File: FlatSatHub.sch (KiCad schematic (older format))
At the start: 15 parts, among them J1 Jack-DC, SW1 SW_DIP_x02, SW10 SW_SPST

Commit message: route and add documentation for schematic
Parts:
- gave numbers to parts that had none: 6
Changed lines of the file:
@@
 F 1 "bel-xRBA-06E2Ax" H 9025 2250 50  0000 L CNN
 F 2 "FlatSatHub:BEL-xRBA-06E2Ax" H 9750 2125 50  0001 C CNN
-F 3 "" H 9750 2125 50  0001 C CNN
+F 3 "https://www.mouser.fr/ProductDetail/Bel-Fuse/SRBA-06E2ALG?qs=sGAEpiMZZMsc0tfZmXiUnbbQTgs0Rw32i9gRZ8J9EPVOGBp8LJLa%2Fg%3D%3D" H 9750 2125 50  0001 C CNN
 	1    9450 1925
 	-1   0    0    1
@@
 F 1 "CINCON-SIPSMT10-12" H 9000 3400 50  0000 L CNN
 F 2 "FlatSatHub:CINCON-SIPSMT10-12" H 10050 3150 50  0001 C CNN
-F 3 "" H 10050 3150 50  0001 C CNN
+F 3 "https://www.mouser.fr/ProductDetail/Cincon/SIP10-12S33?qs=sGAEpiMZZMsc0tfZmXiUnRxObuznqcoYDYuJZBYUaXE=" H 10050 3150 50  0001 C CNN
 	1    9500 3000
 	-1   0    0    1
@@
 $EndComp
 $Comp
-L Device:LED D?
+L Device:LED D3
 U 1 1 5F2D3A02
 P 7850 1600
-F 0 "D?" H 7843 1345 50  0000 C CNN
+F 0 "D3" H 7843 1345 50  0000 C CNN
 F 1 "LED" H 7843 1436 50  0000 C CNN
 F 2 "" H 7850 1600 50  0001 C CNN
@@
 $EndComp
 $Comp
-L Device:LED D?
+L Device:LED D1
 U 1 1 5F2D4A24
 P 7825 2250
-F 0 "D?" H 7818 1995 50  0000 C CNN
+F 0 "D1" H 7818 1995 50  0000 C CNN
 F 1 "LED" H 7818 2086 50  0000 C CNN
 F 2 "" H 7825 2250 50  0001 C CNN
@@
 $EndComp
 $Comp
-L Device:LED D?
+L Device:LED D2
 U 1 1 5F2DEAA8
 P 7825 2575
-F 0 "D?" H 7818 2320 50  0000 C CNN
+F 0 "D2" H 7818 2320 50  0000 C CNN
 F 1 "LED" H 7818 2411 50  0000 C CNN
 F 2 "" H 7825 2575 50  0001 C CNN
@@
 $EndComp
 $Comp
-L Device:R R?
+L Device:R R3
 U 1 1 5F2E82E2
 P 8150 1600
-F 0 "R?" V 7943 1600 50  0000 C CNN
+F 0 "R3" V 7943 1600 50  0000 C CNN
 F 1 "R" V 8034 1600 50  0000 C CNN
 F 2 "" V 8080 1600 50  0001 C CNN
@@
 $EndComp
 $Comp
-L Device:R R?
+L Device:R R1
 U 1 1 5F2E9255
 P 8125 2250
-F 0 "R?" V 7918 2250 50  0000 C CNN
+F 0 "R1" V 7918 2250 50  0000 C CNN
 F 1 "R" V 8009 2250 50  0000 C CNN
 F 2 "" V 8055 2250 50  0001 C CNN
@@
 $EndComp
 $Comp
-L Device:R R?
+L Device:R R2
 U 1 1 5F2F2A98
 P 8125 2575
-F 0 "R?" V 7918 2575 50  0000 C CNN
+F 0 "R2" V 7918 2575 50  0000 C CNN
 F 1 "R" V 8009 2575 50  0000 C CNN
 F 2 "" V 8055 2575 50  0001 C CNN
@@
 $EndComp
 $Comp
-L power:GND #PWR?
+L power:GND #PWR0101
 U 1 1 5F2FC3AF
 P 8300 1600
-F 0 "#PWR?" H 8300 1350 50  0001 C CNN
+F 0 "#PWR0101" H 8300 1350 50  0001 C CNN
 F 1 "GND" V 8305 1472 50  0000 R CNN
 F 2 "" H 8300 1600 50  0001 C CNN
@@
 $EndComp
 $Comp
-L power:GND #PWR?
+L power:GND #PWR0104
 U 1 1 5F2FCCF0
 P 8275 2250
-F 0 "#PWR?" H 8275 2000 50  0001 C CNN
+F 0 "#PWR0104" H 8275 2000 50  0001 C CNN
 F 1 "GND" V 8280 2122 50  0000 R CNN
 F 2 "" H 8275 2250 50  0001 C CNN
@@
 $EndComp
 $Comp
-L power:GND #PWR?
+L power:GND #PWR0107
 U 1 1 5F3063BD
 P 8275 2575
-F 0 "#PWR?" H 8275 2325 50  0001 C CNN
+F 0 "#PWR0107" H 8275 2325 50  0001 C CNN
 F 1 "GND" V 8280 2447 50  0000 R CNN
 F 2 "" H 8275 2575 50  0001 C CNN

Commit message: Change DB-26-HD footprint to match what we want
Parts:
- D1, D2, D3: footprint (none) -> LED_SMD:LED_0603_1608Metric_Pad1.05x0.95mm_HandSolder
- R1, R2, R3: footprint (none) -> Resistor_SMD:R_0603_1608Metric_Pad1.05x0.95mm_HandSolder
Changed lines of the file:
@@
 F 0 "D3" H 7843 1345 50  0000 C CNN
 F 1 "LED" H 7843 1436 50  0000 C CNN
-F 2 "" H 7850 1600 50  0001 C CNN
+F 2 "LED_SMD:LED_0603_1608Metric_Pad1.05x0.95mm_HandSolder" H 7850 1600 50  0001 C CNN
 F 3 "~" H 7850 1600 50  0001 C CNN
 	1    7850 1600
@@
 F 0 "D1" H 7818 1995 50  0000 C CNN
 F 1 "LED" H 7818 2086 50  0000 C CNN
-F 2 "" H 7825 2250 50  0001 C CNN
+F 2 "LED_SMD:LED_0603_1608Metric_Pad1.05x0.95mm_HandSolder" H 7825 2250 50  0001 C CNN
 F 3 "~" H 7825 2250 50  0001 C CNN
 	1    7825 2250
@@
 F 0 "D2" H 7818 2320 50  0000 C CNN
 F 1 "LED" H 7818 2411 50  0000 C CNN
-F 2 "" H 7825 2575 50  0001 C CNN
+F 2 "LED_SMD:LED_0603_1608Metric_Pad1.05x0.95mm_HandSolder" H 7825 2575 50  0001 C CNN
 F 3 "~" H 7825 2575 50  0001 C CNN
 	1    7825 2575
@@
 F 0 "R3" V 7943 1600 50  0000 C CNN
 F 1 "R" V 8034 1600 50  0000 C CNN
-F 2 "" V 8080 1600 50  0001 C CNN
+F 2 "Resistor_SMD:R_0603_1608Metric_Pad1.05x0.95mm_HandSolder" V 8080 1600 50  0001 C CNN
 F 3 "~" H 8150 1600 50  0001 C CNN
 	1    8150 1600
@@
 F 0 "R1" V 7918 2250 50  0000 C CNN
 F 1 "R" V 8009 2250 50  0000 C CNN
-F 2 "" V 8055 2250 50  0001 C CNN
+F 2 "Resistor_SMD:R_0603_1608Metric_Pad1.05x0.95mm_HandSolder" V 8055 2250 50  0001 C CNN
 F 3 "~" H 8125 2250 50  0001 C CNN
 	1    8125 2250
@@
 F 0 "R2" V 7918 2575 50  0000 C CNN
 F 1 "R" V 8009 2575 50  0000 C CNN
-F 2 "" V 8055 2575 50  0001 C CNN
+F 2 "Resistor_SMD:R_0603_1608Metric_Pad1.05x0.95mm_HandSolder" V 8055 2575 50  0001 C CNN
 F 3 "~" H 8125 2575 50  0001 C CNN
 	1    8125 2575

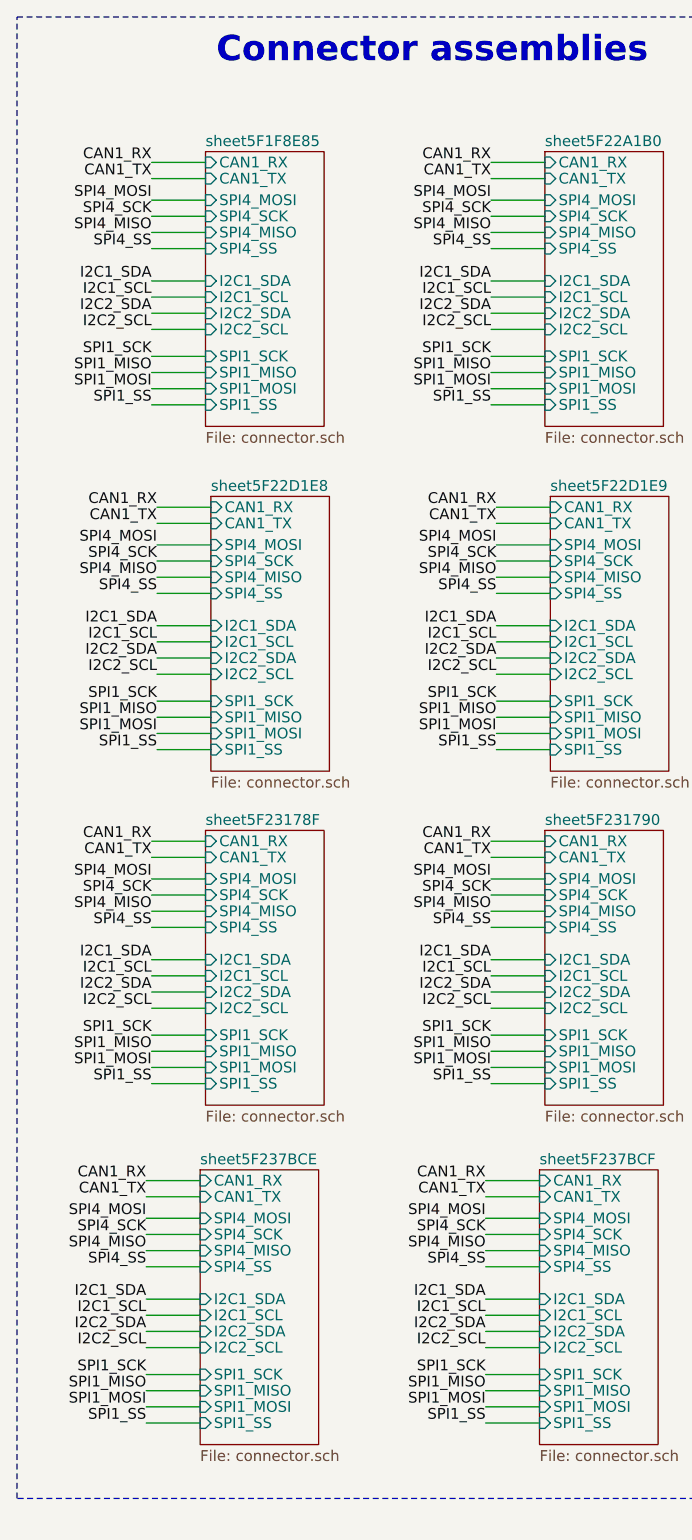
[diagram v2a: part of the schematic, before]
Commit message: new UART layout and rewire
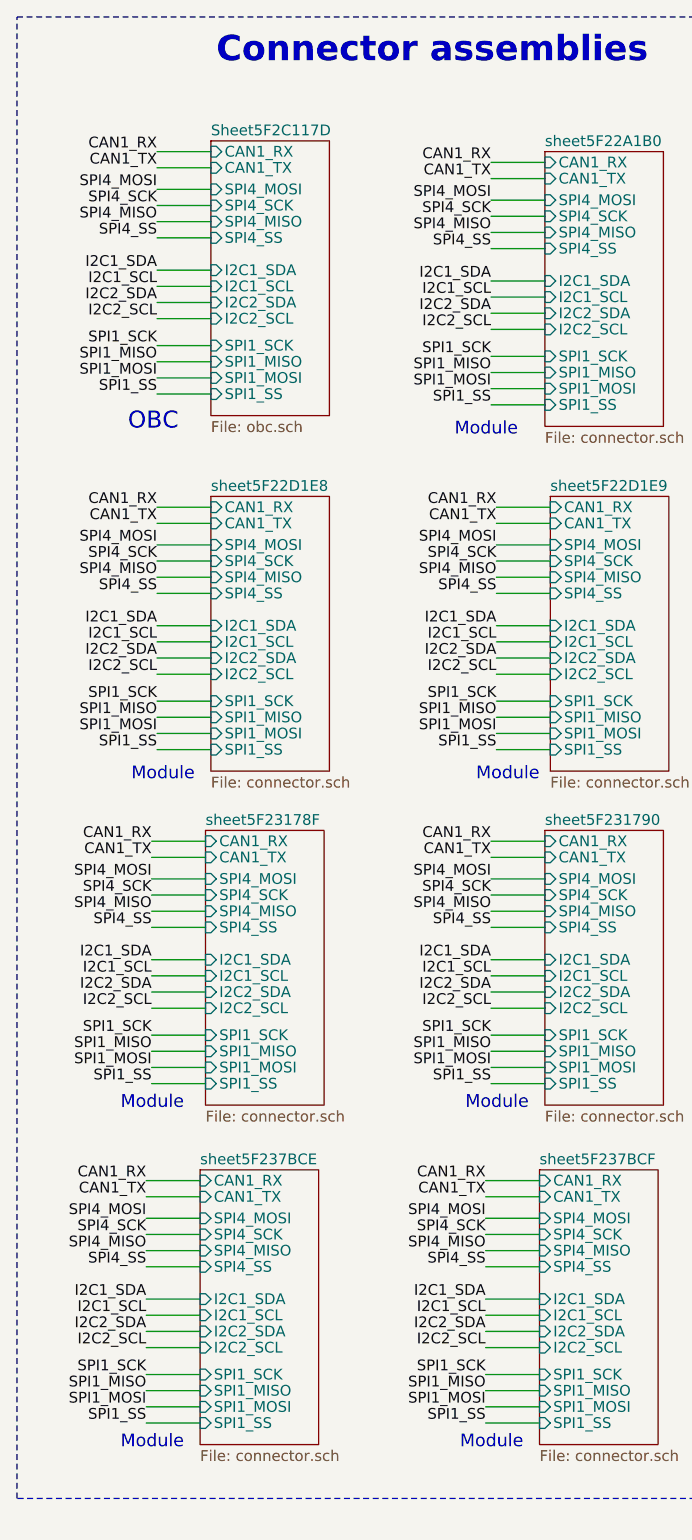
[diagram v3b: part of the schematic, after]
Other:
- note added: "Module"
- note added: "OBC"
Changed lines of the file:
@@
 $EndBitmap
-Wire Wire Line
-	1675 2450 1925 2450
-Wire Wire Line
-	1675 2375 1925 2375
-Wire Wire Line
-	1925 2300 1675 2300
-Wire Wire Line
-	1675 2225 1925 2225
-Wire Wire Line
-	1675 2100 1925 2100
-Wire Wire Line
-	1675 2025 1925 2025
-Wire Wire Line
-	1675 1950 1925 1950
-Wire Wire Line
-	1675 1875 1925 1875
-Wire Wire Line
-	1675 1725 1925 1725
-Wire Wire Line
-	1675 1650 1925 1650
-Wire Wire Line
-	1675 1575 1925 1575
-Wire Wire Line
-	1675 1500 1925 1500
-Wire Wire Line
-	1675 1400 1925 1400
-Wire Wire Line
-	1675 1325 1925 1325
-$Sheet
-S 1925 1275 550  1275
-U 5F1F8EB1
-F0 "sheet5F1F8E85" 50
-F1 "connector.sch" 50
-F2 "I2C1_SDA" I L 1925 1875 50
-F3 "I2C1_SCL" I L 1925 1950 50
-F4 "I2C2_SDA" I L 1925 2025 50
-F5 "SPI1_SCK" I L 1925 2225 50
-F6 "I2C2_SCL" I L 1925 2100 50
-F7 "SPI1_MISO" I L 1925 2300 50
-F8 "SPI1_MOSI" I L 1925 2375 50
-F9 "SPI4_SCK" I L 1925 1575 50
-F10 "SPI4_MISO" I L 1925 1650 50
-F11 "CAN1_RX" I L 1925 1325 50
-F12 "CAN1_TX" I L 1925 1400 50
-F13 "SPI4_MOSI" I L 1925 1500 50
-F14 "SPI1_SS" I L 1925 2450 50
-F15 "SPI4_SS" I L 1925 1725 50
-$EndSheet
-Text Label 1675 1325 2    50   ~ 0
-CAN1_RX
-Text Label 1675 1400 2    50   ~ 0
-CAN1_TX
-Text Label 1675 1500 2    50   ~ 0
-SPI4_MOSI
-Text Label 1675 1575 2    50   ~ 0
-SPI4_SCK
-Text Label 1675 1650 2    50   ~ 0
-SPI4_MISO
-Text Label 1675 1725 2    50   ~ 0
-SPI4_SS
-Text Label 1675 1875 2    50   ~ 0
-I2C1_SDA
-Text Label 1675 1950 2    50   ~ 0
-I2C1_SCL
-Text Label 1675 2025 2    50   ~ 0
-I2C2_SDA
-Text Label 1675 2100 2    50   ~ 0
-I2C2_SCL
-Text Label 1675 2225 2    50   ~ 0
-SPI1_SCK
-Text Label 1675 2300 2    50   ~ 0
-SPI1_MISO
-Text Label 1675 2375 2    50   ~ 0
-SPI1_MOSI
-Text Label 1675 2450 2    50   ~ 0
-SPI1_SS
 Wire Wire Line
 	3250 2450 3500 2450
@@
 Wire Wire Line
 	7600 2450 7525 2450
+Wire Wire Line
+	1700 2400 1950 2400
+Wire Wire Line
+	1700 2325 1950 2325
+Wire Wire Line
+	1950 2250 1700 2250
+Wire Wire Line
+	1700 2175 1950 2175
+Wire Wire Line
+	1700 2050 1950 2050
+Wire Wire Line
+	1700 1975 1950 1975
+Wire Wire Line
+	1700 1900 1950 1900
+Wire Wire Line
+	1700 1825 1950 1825
+Wire Wire Line
+	1700 1675 1950 1675
+Wire Wire Line
+	1700 1600 1950 1600
+Wire Wire Line
+	1700 1525 1950 1525
+Wire Wire Line
+	1700 1450 1950 1450
+Wire Wire Line
+	1700 1350 1950 1350
+Wire Wire Line
+	1700 1275 1950 1275
+Text Label 1700 1275 2    50   ~ 0
+CAN1_RX
+Text Label 1700 1350 2    50   ~ 0
+CAN1_TX
+Text Label 1700 1450 2    50   ~ 0
+SPI4_MOSI
+Text Label 1700 1525 2    50   ~ 0
+SPI4_SCK
+Text Label 1700 1600 2    50   ~ 0
+SPI4_MISO
+Text Label 1700 1675 2    50   ~ 0
+SPI4_SS
+Text Label 1700 1825 2    50   ~ 0
+I2C1_SDA
+Text Label 1700 1900 2    50   ~ 0
+I2C1_SCL
+Text Label 1700 1975 2    50   ~ 0
+I2C2_SDA
+Text Label 1700 2050 2    50   ~ 0
+I2C2_SCL
+Text Label 1700 2175 2    50   ~ 0
+SPI1_SCK
+Text Label 1700 2250 2    50   ~ 0
+SPI1_MISO
+Text Label 1700 2325 2    50   ~ 0
+SPI1_MOSI
+Text Label 1700 2400 2    50   ~ 0
+SPI1_SS
+$Sheet
+S 1950 1225 550  1275
+U 5F2C117D
+F0 "Sheet5F2C117D" 50
+F1 "obc.sch" 50
+F2 "I2C1_SDA" I L 1950 1825 50
+F3 "I2C1_SCL" I L 1950 1900 50
+F4 "I2C2_SDA" I L 1950 1975 50
+F5 "SPI1_SCK" I L 1950 2175 50
+F6 "I2C2_SCL" I L 1950 2050 50
+F7 "SPI1_MISO" I L 1950 2250 50
+F8 "SPI1_MOSI" I L 1950 2325 50
+F9 "SPI4_SCK" I L 1950 1525 50
+F10 "SPI4_MISO" I L 1950 1600 50
+F11 "CAN1_RX" I L 1950 1275 50
+F12 "CAN1_TX" I L 1950 1350 50
+F13 "SPI4_MOSI" I L 1950 1450 50
+F14 "SPI1_SS" I L 1950 2400 50
+F15 "SPI4_SS" I L 1950 1675 50
+$EndSheet
+Text Notes 1800 2575 2    79   ~ 0
+OBC
+Text Notes 3375 2600 2    59   ~ 0
+Module
+Text Notes 3475 4200 2    59   ~ 0
+Module
+Text Notes 1875 4200 2    59   ~ 0
+Module
+Text Notes 3425 5725 2    59   ~ 0
+Module
+Text Notes 1825 5725 2    59   ~ 0
+Module
+Text Notes 1825 7300 2    59   ~ 0
+Module
+Text Notes 3400 7300 2    59   ~ 0
+Module
 $EndSCHEMATC

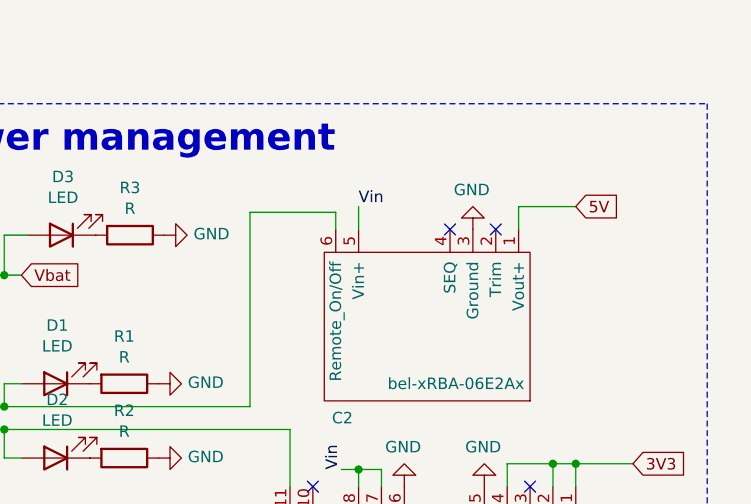
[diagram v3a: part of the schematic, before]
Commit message: fix dc converter wiring and gnd track size
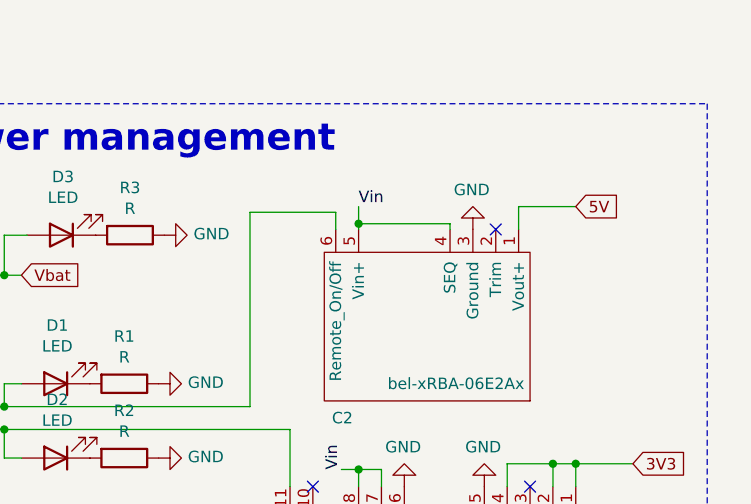
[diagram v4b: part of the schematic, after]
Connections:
- net Vin: now also C2.4 (SEQ)
- no-connect marks 4 -> 3
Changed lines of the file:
@@
 	9150 2700 9150 2625
 Wire Wire Line
-	9150 1575 9150 1475
+	9150 1575 9150 1550
 Wire Wire Line
 	9250 2625 9150 2625
@@
 	9850 1475 10100 1475
 NoConn ~ 9750 1575
-NoConn ~ 9550 1575
 $Comp
 L power:GND #PWR010
@@
 Text Notes 3400 7300 2    59   ~ 0
 Module
+Wire Wire Line
+	9150 1550 9550 1550
+Wire Wire Line
+	9550 1550 9550 1575
+Connection ~ 9150 1550
+Wire Wire Line
+	9150 1550 9150 1475
 $EndSCHEMATC

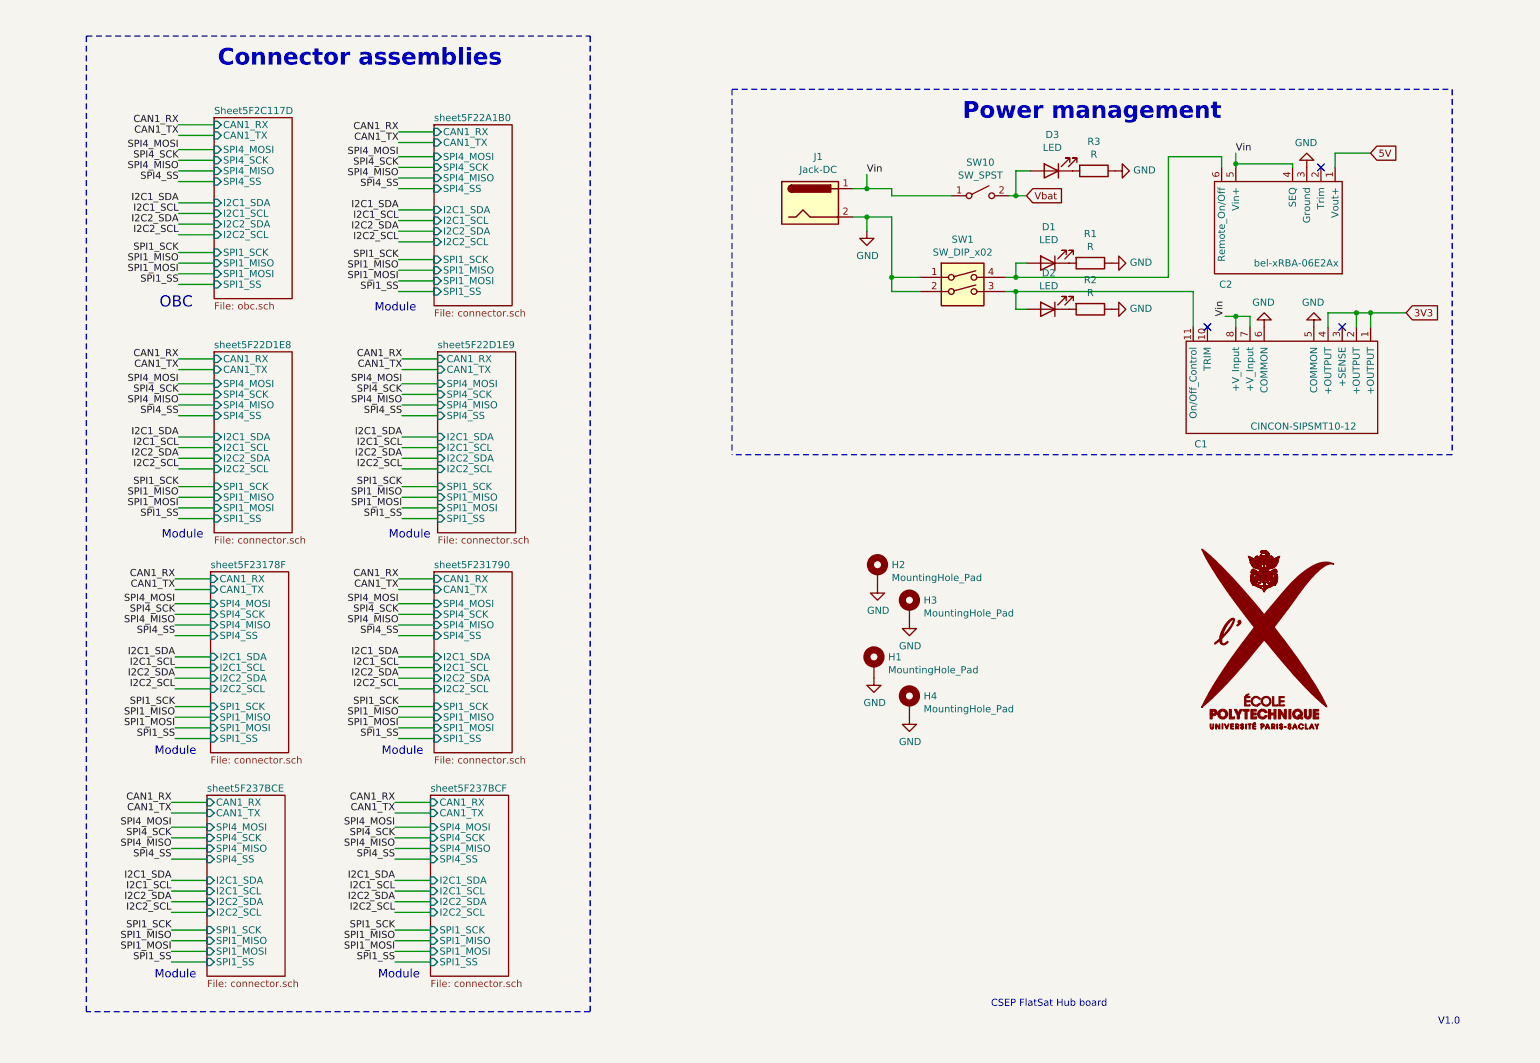
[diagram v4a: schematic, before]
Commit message: New layout with FPGA
- Added FPGA to ease UART and SPI signals routing
- Cleaned layout using start and circle patterns for remaining signals
- Replaced DCDC modules with better TI components

Missing stuff:
- per module PSU switch
- spare FPGA IOs connector?
- silk screen
- ...

Signed-off-by: Alexis Jeandet <alexis.jeandet@member.fsf.org>
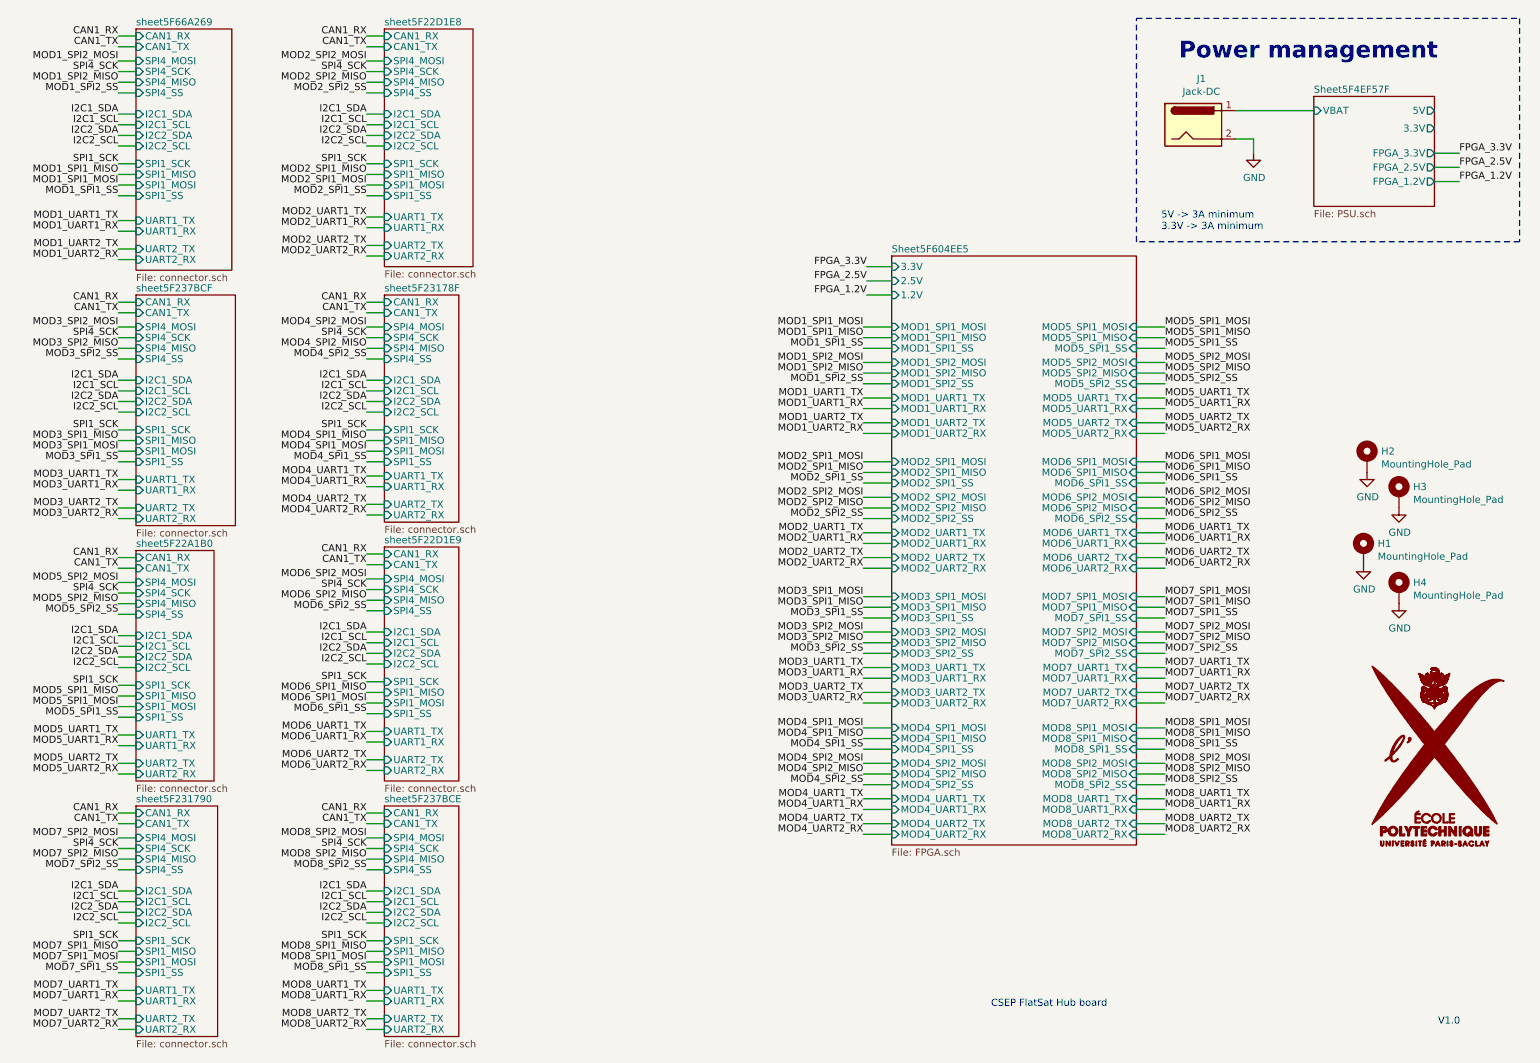
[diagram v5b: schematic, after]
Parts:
- removed C1: CINCON-SIPSMT10-12, FlatSatHub:CINCON-SIPSMT10-12, symbol FlatSatHub:CINCON-SIPSMT10-12
- removed C2: bel-xRBA-06E2Ax, FlatSatHub:BEL-xRBA-06E2Ax, symbol FlatSatHub:bel-xRBA-06E2Ax
- removed D1, D2, D3: LED, LED_SMD:LED_0603_1608Metric_Pad1.05x0.95mm_HandSolder, symbol Device:LED
- removed R1, R2, R3: R, Resistor_SMD:R_0603_1608Metric_Pad1.05x0.95mm_HandSolder, symbol Device:R
- removed SW1: SW_DIP_x02, Button_Switch_THT:SW_DIP_SPSTx02_Slide_6.7x6.64mm_W7.62mm_P2.54mm_LowProfile, symbol Switch:SW_DIP_x02
- removed SW10: SW_SPST, Button_Switch_THT:SW_DIP_SPSTx01_Slide_9.78x4.72mm_W7.62mm_P2.54mm, symbol Switch:SW_SPST
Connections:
- net Vin renamed Sheet5F4EF57F/VBAT
- no-connect marks 3 -> 0
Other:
- note added: "5V -> 3A minimum\n3.3V -> 3A minimum"
- note removed: "Connector assemblies"
- note removed: "Module"
- note removed: "OBC"
- moved on the sheet: H1, H2, H3, H4, J1
